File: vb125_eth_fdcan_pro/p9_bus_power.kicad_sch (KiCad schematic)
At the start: 44 parts, among them T2 750315125, U14 LV14360SDDAR, U15 LT8304IS8E#PBF

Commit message: Add sourcing information for resistors
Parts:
- R19: Mpn1 (none) -> CR0402-FX-1000GLF; Mpn2 (none) -> RMCF0402FT100R
- R19: Mpn1 (none) -> RMCF0402FT158K; Mpn2 (none) -> RC0402FR-07158KL
- R19: Mpn1 (none) -> RMCF0402FT348K; Mpn2 (none) -> RC0402FR-07348KL
- R19: Mpn1 (none) -> RM04F1002CT; Mpn2 (none) -> RMCF0402FT10K0; Mpn3 (none) -> CR0402-FX-1002GLF
- R19: Mpn1 (none) -> CR0402-FX-1004GLF; Mpn2 (none) -> RMCF0402FT1M00
- R19: Mpn1 (none) -> RMCF0402FT57K6; Mpn2 (none) -> RC0402FR-0757K6L; Mpn3 (none) -> AC0402FR-0757K6L
- R19: Mpn1 (none) -> RMCF0402FT49K9; Mpn2 (none) -> CR0402-FX-4992GLF
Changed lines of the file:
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@@
+      (effects (font (size 1.27 1.27)) hide)
+    )
+    (property "Mpn1" "CR0402-FX-1000GLF" (at 220.98 86.36 0)
+      (effects (font (size 1.27 1.27)) hide)
+    )
+    (property "Mpn2" "RMCF0402FT100R" (at 220.98 86.36 0)
       (effects (font (size 1.27 1.27)) hide)
     )
@@
     )
     (property "Datasheet" "~" (at 220.98 101.6 0)
+      (effects (font (size 1.27 1.27)) hide)
+    )
+    (property "Mpn1" "RMCF0402FT158K" (at 220.98 101.6 0)
+      (effects (font (size 1.27 1.27)) hide)
+    )
+    (property "Mpn2" "RC0402FR-07158KL" (at 220.98 101.6 0)
       (effects (font (size 1.27 1.27)) hide)
     )
@@
       (effects (font (size 1.27 1.27)) hide)
     )
+    (property "Mpn1" "RMCF0402FT348K" (at 149.86 123.19 0)
+      (effects (font (size 1.27 1.27)) hide)
+    )
+    (property "Mpn2" "RC0402FR-07348KL" (at 149.86 123.19 0)
+      (effects (font (size 1.27 1.27)) hide)
+    )
     (pin "1")
     (pin "2")
@@
       (effects (font (size 1.27 1.27)) hide)
     )
+    (property "Mpn1" "RM04F1002CT" (at 209.55 123.19 0)
+      (effects (font (size 1.27 1.27)) hide)
+    )
+    (property "Mpn2" "RMCF0402FT10K0" (at 209.55 123.19 0)
+      (effects (font (size 1.27 1.27)) hide)
+    )
+    (property "Mpn3" "CR0402-FX-1002GLF" (at 209.55 123.19 0)
+      (effects (font (size 1.27 1.27)) hide)
+    )
     (pin "1")
     (pin "2")
@@
     )
     (property "Datasheet" "~" (at 153.67 167.64 0)
+      (effects (font (size 1.27 1.27)) hide)
+    )
+    (property "Mpn1" "RM04F1002CT" (at 153.67 167.64 0)
+      (effects (font (size 1.27 1.27)) hide)
+    )
+    (property "Mpn2" "RMCF0402FT10K0" (at 153.67 167.64 0)
+      (effects (font (size 1.27 1.27)) hide)
+    )
+    (property "Mpn3" "CR0402-FX-1002GLF" (at 153.67 167.64 0)
       (effects (font (size 1.27 1.27)) hide)
     )
@@
       (effects (font (size 1.27 1.27)) hide)
     )
+    (property "Mpn1" "RM04F1002CT" (at 246.38 186.69 0)
+      (effects (font (size 1.27 1.27)) hide)
+    )
+    (property "Mpn2" "RMCF0402FT10K0" (at 246.38 186.69 0)
+      (effects (font (size 1.27 1.27)) hide)
+    )
+    (property "Mpn3" "CR0402-FX-1002GLF" (at 246.38 186.69 0)
+      (effects (font (size 1.27 1.27)) hide)
+    )
     (pin "1")
     (pin "2")
@@
     )
     (property "Datasheet" "~" (at 149.86 97.79 0)
+      (effects (font (size 1.27 1.27)) hide)
+    )
+    (property "Mpn1" "CR0402-FX-1004GLF" (at 149.86 97.79 0)
+      (effects (font (size 1.27 1.27)) hide)
+    )
+    (property "Mpn2" "RMCF0402FT1M00" (at 149.86 97.79 0)
       (effects (font (size 1.27 1.27)) hide)
     )
@@
     )
     (property "Datasheet" "~" (at 246.38 173.99 0)
+      (effects (font (size 1.27 1.27)) hide)
+    )
+    (property "Mpn1" "RMCF0402FT57K6" (at 246.38 173.99 0)
+      (effects (font (size 1.27 1.27)) hide)
+    )
+    (property "Mpn2" "RC0402FR-0757K6L" (at 246.38 173.99 0)
+      (effects (font (size 1.27 1.27)) hide)
+    )
+    (property "Mpn3" "AC0402FR-0757K6L" (at 246.38 173.99 0)
       (effects (font (size 1.27 1.27)) hide)
     )
@@
       (effects (font (size 1.27 1.27)) hide)
     )
+    (property "Mpn1" "RMCF0402FT49K9" (at 147.32 186.69 0)
+      (effects (font (size 1.27 1.27)) hide)
+    )
+    (property "Mpn2" "CR0402-FX-4992GLF" (at 147.32 186.69 0)
+      (effects (font (size 1.27 1.27)) hide)
+    )

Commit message: Add variants.
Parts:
- C1, C63, C66, D19, D20, D22, D23, R19, T2, U15: Variant (none) -> bp_iso
- C1, C2, C20, C63, C66, D21, L6, R19, U14: Variant (none) -> bp_dc
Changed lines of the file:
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@@
+      (effects (font (size 1.27 1.27)) hide)
+    )
+    (property "Variant" "bp_iso" (at 196.85 73.66 0)
       (effects (font (size 1.27 1.27)) hide)
     )
@@
     )
     (property "Field8" "" (at 220.98 73.66 0)
+      (effects (font (size 1.27 1.27)) hide)
+    )
+    (property "Variant" "bp_iso" (at 220.98 73.66 0)
       (effects (font (size 1.27 1.27)) hide)
     )
@@
     )
     (property "Vworking" "3.3V" (at 209.55 162.56 0)
+      (effects (font (size 1.27 1.27)) hide)
+    )
+    (property "Variant" "bp_dc" (at 209.55 162.56 0)
       (effects (font (size 1.27 1.27)) hide)
     )
@@
       (effects (font (size 1.27 1.27)) (justify left))
     )
+    (property "Variant" "bp_iso" (at 138.43 106.68 0)
+      (effects (font (size 1.27 1.27)) hide)
+    )
     (pin "1")
     (pin "2")
@@
       (effects (font (size 1.27 1.27)) hide)
     )
+    (property "Variant" "bp_iso" (at 308.61 81.28 0)
+      (effects (font (size 1.27 1.27)) hide)
+    )
     (pin "1")
     (pin "2")
@@
     )
     (property "Vworking" "3.3V" (at 157.48 186.69 0)
+      (effects (font (size 1.27 1.27)) hide)
+    )
+    (property "Variant" "bp_dc" (at 157.48 186.69 0)
       (effects (font (size 1.27 1.27)) hide)
     )
@@
       (effects (font (size 1.27 1.27)) hide)
     )
+    (property "Variant" "bp_iso" (at 220.98 86.36 0)
+      (effects (font (size 1.27 1.27)) hide)
+    )
     (pin "1")
     (pin "2")
@@
       (effects (font (size 1.27 1.27)) (justify left))
     )
+    (property "Variant" "bp_dc" (at 119.38 186.69 0)
+      (effects (font (size 1.27 1.27)) hide)
+    )
     (pin "1")
     (pin "2")
@@
       (effects (font (size 1.27 1.27)) hide)
     )
+    (property "Variant" "bp_iso" (at 220.98 101.6 0)
+      (effects (font (size 1.27 1.27)) hide)
+    )
     (pin "1")
     (pin "2")
@@
     )
     (property "Irated" "3A" (at 262.89 73.66 0)
+      (effects (font (size 1.27 1.27)) hide)
+    )
+    (property "Variant" "bp_iso" (at 262.89 73.66 0)
       (effects (font (size 1.27 1.27)) hide)
     )
@@
     )
     (property "Description" "100VIN Micropower No-Opto Isolated Flyback Converter with 150V/2A Switch" (at 181.6149 99.06 0)
+      (effects (font (size 1.27 1.27)) hide)
+    )
+    (property "Variant" "bp_iso" (at 173.99 100.33 0)
       (effects (font (size 1.27 1.27)) hide)
     )
@@
       (effects (font (size 1.27 1.27)) (justify left))
     )
+    (property "Variant" "bp_iso" (at 294.64 81.28 0)
+      (effects (font (size 1.27 1.27)) hide)
+    )
     (pin "1")
     (pin "2")
@@
     )
     (property "Field8" "" (at 158.75 123.19 0)
+      (effects (font (size 1.27 1.27)) hide)
+    )
+    (property "Variant" "bp_iso" (at 158.75 123.19 0)
       (effects (font (size 1.27 1.27)) hide)
     )
@@
       (effects (font (size 1.27 1.27)) hide)
     )
+    (property "Variant" "bp_iso" (at 149.86 123.19 0)
+      (effects (font (size 1.27 1.27)) hide)
+    )
     (pin "1")
     (pin "2")
@@
       (effects (font (size 1.27 1.27)) (justify left))
     )
+    (property "Variant" "bp_iso" (at 281.94 81.28 0)
+      (effects (font (size 1.27 1.27)) hide)
+    )
     (pin "1")
     (pin "2")
@@
       (effects (font (size 1.27 1.27)) hide)
     )
+    (property "Variant" "bp_dc" (at 212.09 186.69 0)
+      (effects (font (size 1.27 1.27)) hide)
+    )
     (pin "1")
     (pin "2")
@@
     (property "Package" "1210" (at 107.315 109.22 0)
       (effects (font (size 1.27 1.27)) (justify left))
+    )
+    (property "Variant" "bp_iso" (at 104.14 106.68 0)
+      (effects (font (size 1.27 1.27)) hide)
     )
     (pin "1")
@@
       (effects (font (size 1.27 1.27)) hide)
     )
+    (property "Variant" "bp_dc" (at 228.6 167.64 0)
+      (effects (font (size 1.27 1.27)) hide)
+    )
     (pin "1")
     (pin "2")
@@
     )
     (property "Mpn3" "CR0402-FX-1002GLF" (at 209.55 123.19 0)
+      (effects (font (size 1.27 1.27)) hide)
+    )
+    (property "Variant" "bp_iso" (at 209.55 123.19 0)
       (effects (font (size 1.27 1.27)) hide)
     )
@@
       (effects (font (size 1.27 1.27)) hide)
     )
+    (property "Variant" "bp_dc" (at 153.67 167.64 0)
+      (effects (font (size 1.27 1.27)) hide)
+    )
     (pin "1")
     (pin "2")
@@
       (effects (font (size 1.27 1.27)) (justify left))
     )
+    (property "Variant" "bp_dc" (at 260.35 186.69 0)
+      (effects (font (size 1.27 1.27)) hide)
+    )
     (pin "1")
     (pin "2")
@@
     )
     (property "Field8" "" (at 132.08 186.69 0)
+      (effects (font (size 1.27 1.27)) hide)
+    )
+    (property "Variant" "bp_dc" (at 132.08 186.69 0)
       (effects (font (size 1.27 1.27)) hide)
     )
@@
     )
     (property "Datasheet" "https://www.ti.com/lit/ds/symlink/lv14360.pdf" (at 173.99 187.96 0)
+      (effects (font (size 1.27 1.27)) hide)
+    )
+    (property "Variant" "bp_dc" (at 171.45 160.02 0)
       (effects (font (size 1.27 1.27)) hide)
     )
@@
       (effects (font (size 1.27 1.27)) hide)
     )
+    (property "Variant" "bp_dc" (at 246.38 186.69 0)
+      (effects (font (size 1.27 1.27)) hide)
+    )
     (pin "1")
     (pin "2")
@@
     )
     (property "Mpn2" "RMCF0402FT1M00" (at 149.86 97.79 0)
+      (effects (font (size 1.27 1.27)) hide)
+    )
+    (property "Variant" "bp_iso" (at 149.86 97.79 0)
       (effects (font (size 1.27 1.27)) hide)
     )
@@
       (effects (font (size 1.27 1.27)) hide)
     )
+    (property "Variant" "bp_iso" (at 318.77 82.55 0)
+      (effects (font (size 1.27 1.27)) hide)
+    )
     (pin "1")
     (pin "2")
@@
     )
     (property "Mpn3" "AC0402FR-0757K6L" (at 246.38 173.99 0)
+      (effects (font (size 1.27 1.27)) hide)
+    )
+    (property "Variant" "bp_dc" (at 246.38 173.99 0)
       (effects (font (size 1.27 1.27)) hide)
     )
@@
       (effects (font (size 1.27 1.27)) hide)
     )
+    (property "Variant" "bp_iso" (at 196.85 86.36 0)
+      (effects (font (size 1.27 1.27)) hide)
+    )
     (pin "1")
     (pin "2")
@@
     )
     (property "Datasheet" "https://media.digikey.com/pdf/Data%20Sheets/Wurth%20Electronics%20PDFs/750315125_Dwg~.pdf" (at 231.14 93.98 0)
+      (effects (font (size 1.27 1.27)) hide)
+    )
+    (property "Variant" "bp_iso" (at 241.3 71.12 0)
       (effects (font (size 1.27 1.27)) hide)
     )
@@
       (effects (font (size 1.27 1.27)) hide)
     )
+    (property "Variant" "bp_iso" (at 200.66 123.19 0)
+      (effects (font (size 1.27 1.27)) hide)
+    )
     (pin "1")
     (pin "2")
@@
       (effects (font (size 1.27 1.27)) (justify left))
     )
+    (property "Variant" "bp_iso" (at 269.24 81.28 0)
+      (effects (font (size 1.27 1.27)) hide)
+    )
     (pin "1")
     (pin "2")
@@
     )
     (property "Mpn2" "CR0402-FX-4992GLF" (at 147.32 186.69 0)
+      (effects (font (size 1.27 1.27)) hide)
+    )
+    (property "Variant" "bp_dc" (at 147.32 186.69 0)
       (effects (font (size 1.27 1.27)) hide)
     )
@@
       (effects (font (size 1.27 1.27)) (justify left))
     )
+    (property "Variant" "bp_iso" (at 127 106.68 0)
+      (effects (font (size 1.27 1.27)) hide)
+    )
     (pin "1")
     (pin "2")
@@
       (effects (font (size 1.27 1.27)) (justify left))
     )
-    (pin "1")
+    (property "Variant" "bp_iso" (at 115.57 106.68 0)
+      (effects (font (size 1.27 1.27)) hide)
+    )
+    (pin "1")

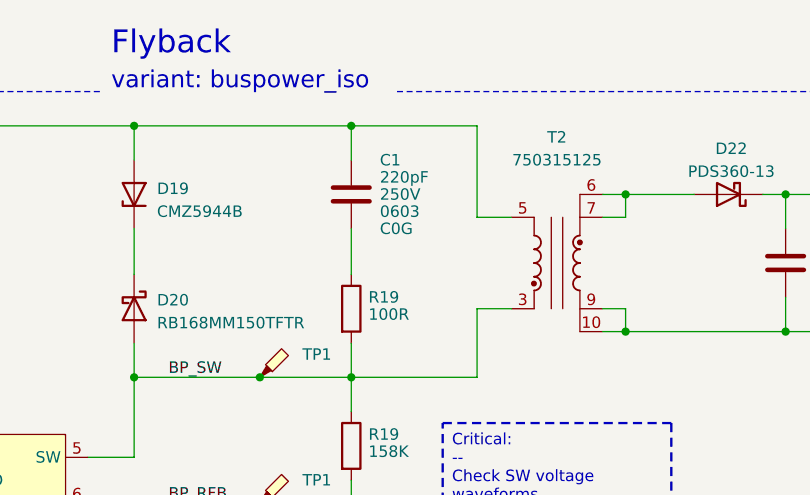
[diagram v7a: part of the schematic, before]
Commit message: Selection of capacitors for VB125
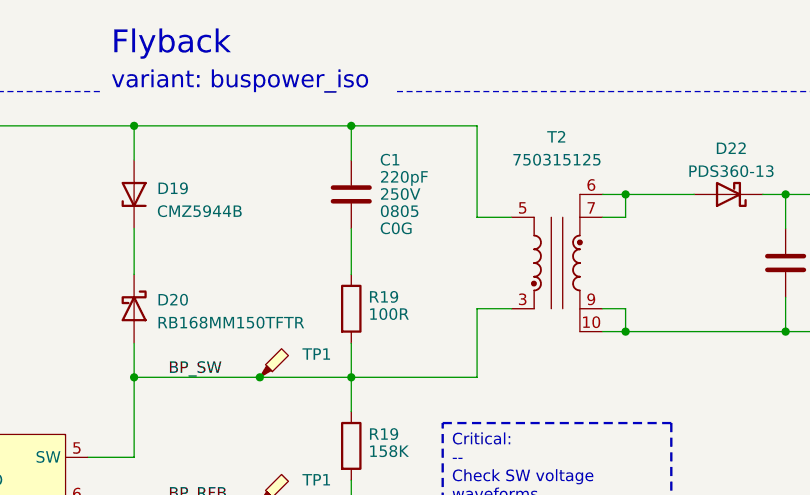
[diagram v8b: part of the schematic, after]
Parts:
- C1: footprint Capacitor_SMD:C_0603_1608Metric -> Capacitor_SMD:C_0805_2012Metric; Mpn1 (none) -> CC0805KRX7RYBB221; Mpn2 (none) -> C0805C221KARAC7800; Package 0603 -> 0805
- C1: Mpn1 (none) -> Murata:GRM155R70J105KA12D; Mpn2 (none) -> Murata:GRM155R70J105KA12J
- C1, C2, C20: Mpn1 (none) -> Samsung:CL05B104KQ5NNNC; Mpn2 (none) -> YAGEO:CC0402KRX7R5BB104
- C63: Mpn2 (none) -> TDK Corporation:CNC6P1X7R2A475K250AE
- C63: Mpn1 Samsung:CL32B106KBJNNNE -> Samsung:CL32B106KBJNNNE - ТАМ КУЧА РАЗНЫХ МОДИФИКАЦИЙ; Mpn2 (none) -> YAGEO:CC1210KKX7R9BB106
- C66: Mpn2 (none) -> Murata:GRM32ER61A107ME20L Samsung:CL32A107MPVNNNE
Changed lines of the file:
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@@
       (effects (font (size 1.27 1.27)) (justify left))
     )
-    (property "Footprint" "Capacitor_SMD:C_0603_1608Metric" (at 221.9452 77.47 0)
+    (property "Footprint" "Capacitor_SMD:C_0805_2012Metric" (at 221.9452 77.47 0)
       (effects (font (size 1.27 1.27)) hide)
     )
@@
       (effects (font (size 1.27 1.27)) (justify left))
     )
-    (property "Package" "0603" (at 224.155 75.565 0)
+    (property "Package" "0805" (at 224.155 75.565 0)
       (effects (font (size 1.27 1.27)) (justify left))
     )
@@
     )
     (property "Variant" "bp_iso" (at 220.98 73.66 0)
+      (effects (font (size 1.27 1.27)) hide)
+    )
+    (property "Mpn1" "CC0805KRX7RYBB221" (at 220.98 73.66 0)
+      (effects (font (size 1.27 1.27)) hide)
+    )
+    (property "Mpn2" "C0805C221KARAC7800" (at 220.98 73.66 0)
       (effects (font (size 1.27 1.27)) hide)
     )
@@
     )
     (property "Variant" "bp_dc" (at 209.55 162.56 0)
+      (effects (font (size 1.27 1.27)) hide)
+    )
+    (property "Mpn1" "Samsung:CL05B104KQ5NNNC  " (at 209.55 162.56 0)
+      (effects (font (size 1.27 1.27)) hide)
+    )
+    (property "Mpn2" "YAGEO:CC0402KRX7R5BB104" (at 209.55 162.56 0)
       (effects (font (size 1.27 1.27)) hide)
     )
@@
       (effects (font (size 1.27 1.27)) hide)
     )
+    (property "Mpn2" "TDK Corporation:CNC6P1X7R2A475K250AE" (at 138.43 106.68 0)
+      (effects (font (size 1.27 1.27)) hide)
+    )
     (pin "1")
     (pin "2")
@@
       (effects (font (size 1.27 1.27)) hide)
     )
+    (property "Mpn1" "Samsung:CL05B104KQ5NNNC  " (at 157.48 186.69 0)
+      (effects (font (size 1.27 1.27)) hide)
+    )
+    (property "Mpn2" "YAGEO:CC0402KRX7R5BB104" (at 157.48 186.69 0)
+      (effects (font (size 1.27 1.27)) hide)
+    )
     (pin "1")
     (pin "2")
@@
       (effects (font (size 1.27 1.27)) (justify left))
     )
-    (property "Mpn1" "Samsung:CL32B106KBJNNNE" (at 119.38 186.69 0)
+    (property "Mpn1" "Samsung:CL32B106KBJNNNE - ТАМ КУЧА РАЗНЫХ МОДИФИКАЦИЙ" (at 119.38 186.69 0)
       (effects (font (size 1.27 1.27)) hide)
     )
@@
     )
     (property "Variant" "bp_dc" (at 119.38 186.69 0)
+      (effects (font (size 1.27 1.27)) hide)
+    )
+    (property "Mpn2" "YAGEO:CC1210KKX7R9BB106" (at 119.38 186.69 0)
       (effects (font (size 1.27 1.27)) hide)
     )
@@
       (effects (font (size 1.27 1.27)) hide)
     )
+    (property "Mpn2" "Murata:GRM32ER61A107ME20L  Samsung:CL32A107MPVNNNE" (at 294.64 81.28 0)
+      (effects (font (size 1.27 1.27)) hide)
+    )
     (pin "1")
     (pin "2")
@@
     )
     (property "Variant" "bp_iso" (at 158.75 123.19 0)
+      (effects (font (size 1.27 1.27)) hide)
+    )
+    (property "Mpn1" "Murata:GRM155R70J105KA12D" (at 158.75 123.19 0)
+      (effects (font (size 1.27 1.27)) hide)
+    )
+    (property "Mpn2" "Murata:GRM155R70J105KA12J" (at 158.75 123.19 0)
       (effects (font (size 1.27 1.27)) hide)
     )
@@
       (effects (font (size 1.27 1.27)) hide)
     )
+    (property "Mpn2" "Murata:GRM32ER61A107ME20L  Samsung:CL32A107MPVNNNE" (at 281.94 81.28 0)
+      (effects (font (size 1.27 1.27)) hide)
+    )
     (pin "1")
     (pin "2")
@@
     )
     (property "Variant" "bp_iso" (at 104.14 106.68 0)
+      (effects (font (size 1.27 1.27)) hide)
+    )
+    (property "Mpn2" "TDK Corporation:CNC6P1X7R2A475K250AE" (at 104.14 106.68 0)
       (effects (font (size 1.27 1.27)) hide)
     )
@@
       (effects (font (size 1.27 1.27)) hide)
     )
+    (property "Mpn2" "Murata:GRM32ER61A107ME20L  Samsung:CL32A107MPVNNNE" (at 260.35 186.69 0)
+      (effects (font (size 1.27 1.27)) hide)
+    )
     (pin "1")
     (pin "2")
@@
     )
     (property "Variant" "bp_dc" (at 132.08 186.69 0)
+      (effects (font (size 1.27 1.27)) hide)
+    )
+    (property "Mpn1" "Samsung:CL05B104KQ5NNNC  " (at 132.08 186.69 0)
+      (effects (font (size 1.27 1.27)) hide)
+    )
+    (property "Mpn2" "YAGEO:CC0402KRX7R5BB104" (at 132.08 186.69 0)
       (effects (font (size 1.27 1.27)) hide)
     )
@@
       (effects (font (size 1.27 1.27)) hide)
     )
+    (property "Mpn2" "Murata:GRM32ER61A107ME20L  Samsung:CL32A107MPVNNNE" (at 269.24 81.28 0)
+      (effects (font (size 1.27 1.27)) hide)
+    )
     (pin "1")
     (pin "2")
@@
       (effects (font (size 1.27 1.27)) hide)
     )
+    (property "Mpn2" "TDK Corporation:CNC6P1X7R2A475K250AE" (at 127 106.68 0)
+      (effects (font (size 1.27 1.27)) hide)
+    )
     (pin "1")
     (pin "2")
@@
       (effects (font (size 1.27 1.27)) hide)
     )
+    (property "Mpn2" "TDK Corporation:CNC6P1X7R2A475K250AE" (at 115.57 106.68 0)
+      (effects (font (size 1.27 1.27)) hide)
+    )
